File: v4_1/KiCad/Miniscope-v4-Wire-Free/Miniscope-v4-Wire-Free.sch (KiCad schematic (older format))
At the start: 92 parts, among them J1 0475710001, J10 Conn_01x01, J2 Conn_01x04, J3 Conn_01x04, J4 Conn_01x01, J5 Conn_01x01, J6 Conn_01x01, J7 Conn_01x01, J8 Conn_01x01, J9 Conn_01x01, Q1 NTK3134NT1G, U1 LTC3554, U2 HV892, U3 LTC3218, U4 MAX13030EETE+BGA, U5 TSOP57438TT1, U6 ATSAMD51J20A-UUT-EFP, U7 NCP163AMX330TBG, U8 NOIP1SN0480A, U9 LMV321IDCKR, Y1 Crystal_GND24, Y2 Crystal_GND24

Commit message: Start routing PCB v4 wire-free
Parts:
- removed C21, C8: 26pF, .Capacitor:C_0201_0603Metric_L, symbol .Device:C_Small
- removed C39: 1uF, .Capacitor:C_0201_0603Metric_L, symbol .Device:C_Small
- removed Y1, Y2: Crystal_GND24, Crystal:Crystal_SMD_2016-4Pin_2.0x1.6mm, symbol Device:Crystal_GND24
- added J14, J15, J16, J17, J18, J19, J20, J21, J22, J23, J24, J25, J26, J27: Conn_01x01, .Connector:Conn_1x1_700_Circular_Pad, symbol Connector_Generic:Conn_01x01
- added Y2: Crystal, Crystal:Crystal_SMD_MicroCrystal_CC8V-T1A-2Pin_2.0x1.2mm, symbol Device:Crystal
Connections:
- net labels added: I_LED, UART_RX, UART_TX
- net labels removed: SD_EN, USB_DM, USB_DP
- wire segments 356 -> 354
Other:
- note added: "Probably add volt div on output. Internal is a 33K res up to VSS"
- note added: "SERCOM5"
- moved on the sheet: C18, C20

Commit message: Do more routing
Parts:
- added D3: LED_Small_ALT, .LED:LED_SC80X160X65L40L, symbol .Device:LED_Small_ALT
- added J11, J12: Conn_01x01, .Connector:Conn_1x1_700_Circular_Pad, symbol Connector_Generic:Conn_01x01
- added R15: 37K, .Resistor:R_0201_0603Metric_ERJ_L, symbol .Device:R_Small_US
- added R16: 100K, .Resistor:R_0201_0603Metric_ERJ_L, symbol .Device:R_Small_US
- added R17: 25K, .Resistor:R_0201_0603Metric_ERJ_L, symbol .Device:R_Small_US
- added R18: R_Small_US, .Resistor:R_0201_0603Metric_ERJ_L, symbol .Device:R_Small_US
- added SW1: TL3780AF330QG, .Switch:SMD-Switch-3mmx2mm, symbol Switch:SW_Push
- D2: footprint (none) -> .LED:LED_SC80X160X65L40L
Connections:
- net USB_D+ is gone; now on net PUSH_BUT_MCU: U6.A1 (PA25)
- net USB_D- is gone; now on net STBY_POWER: U6.B1 (PA24)
- net XIN is gone; now on net IR_REC: U6.A2 (PB22)
- net +1V8: now also J6.1 (Pin_1), U1.9 (PWR_ON1), R16.1; no longer J7.1 (Pin_1)
- net +3V3: now also U1.8 (PWR_ON2), D3.2 (A)
- net BAT+: now also J10.1 (Pin_1); no longer J9.1 (Pin_1)
- net GND: now also J1.G4 (POL), J5.1 (Pin_1), J9.1 (Pin_1), U1.2 (FSEL), J11.1 (Pin_1), J12.1 (Pin_1), R15.2, R18.1, SW1.1; no longer J10.1 (Pin_1), J20.1 (Pin_1), J27.1 (Pin_1), J4.1 (Pin_1)
- net IR_REC: now also R15.1
- net MONITOR0: now also U6.G8 (PA07)
- net RESET_N: now also U6.H4 (PB13)
- net SWCLK: now also J7.1 (Pin_1); no longer J5.1 (Pin_1)
- net SWDIO: now also J4.1 (Pin_1); no longer J6.1 (Pin_1)
- net TRIGGER0: now also U6.H2 (PA15)
- net USB_VBUS: now also R17.2
- net SD_DET: now reaches J1.G5 (DET)
- net SD_DET: now also U6.F8 (PB09)
- net LED_STATUS: now reaches U6.D8 (PB05)
- net at U1.1 (HPWR): now also R17.1
- net STBY_POWER: now reaches U1.10 (STBY)
- net PUSH_BUT_MCU: now reaches U1.3 (PBSTAT)
- net PUSH_BUT_MCU: now also R16.2
- net nON: now reaches U1.5 (nON)
- net nON: now also J20.1 (Pin_1), J27.1 (Pin_1), SW1.2
- net XOUT: no longer names the net of U6.A3 (PB23)
- new net: D3.1 (K), R18.2
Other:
- note added: "Can use side mount LED \nLTST-S270KRKT"
- note added: "Int. pull down res"
- moved on the sheet: J10, J9

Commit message: Finish most of the routing.
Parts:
- added Q2: MMBT3904LP-7B, .Transistor:TRXDFN3_101X61X53L25X15N, symbol .Transistor:MMBT3904LP-7B
- added R19: 1K, .Resistor:R_0201_0603Metric_ERJ_L, symbol .Device:R_Small_US
- added R20: 100K, .Resistor:R_0201_0603Metric_ERJ_L, symbol .Device:R_Small_US
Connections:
- net +1V8: now also J19.1 (Pin_1), J26.1 (Pin_1), R20.2; no longer J15.1 (Pin_1), J22.1 (Pin_1)
- net +3V3: no longer U1.8 (PWR_ON2)
- net GND: now also U1.10 (STBY), Q2.2 (E)
- net I2C_BB_SCL: now also J15.1 (Pin_1), J22.1 (Pin_1); no longer J17.1 (Pin_1), J24.1 (Pin_1)
- net I2C_BB_SDA: now also J16.1 (Pin_1), J23.1 (Pin_1); no longer J18.1 (Pin_1), J25.1 (Pin_1)
- net IR_REC: now also J17.1 (Pin_1), J24.1 (Pin_1); no longer J19.1 (Pin_1), J26.1 (Pin_1)
- net I_LED: now also J18.1 (Pin_1), J25.1 (Pin_1); no longer J16.1 (Pin_1), J23.1 (Pin_1)
- net LED_STATUS: now also U6.F8 (PB09), R19.2; no longer U6.D8 (PB05)
- net SD_DET: now also U6.D8 (PB05); no longer U6.F8 (PB09)
- net UART_RX: now also J2.2 (Pin_2); no longer J2.3 (Pin_3)
- net UART_TX: now also J2.3 (Pin_3); no longer J2.2 (Pin_2)
- net VDC: now also R2.2; no longer D2.2 (A)
- net nCHRG: now reaches U6.A3 (PB23)
- net nCHRG: now also U1.14 (nCHRG), R20.1
- net at R2.1: now also D2.2 (A); no longer D2.1 (K)
- net STBY_POWER renamed 3V3_EN
- net 3V3_EN: now also U1.8 (PWR_ON2); no longer U1.10 (STBY)
- new net: D2.1 (K), Q2.3 (C)
- new net: Q2.1 (B), R19.1
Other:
- note added: "Use EXTINT"
- moved on the sheet: D2, R2
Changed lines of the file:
@@
 	3150 2950 3500 2950
 Connection ~ 3500 2950
-Wire Wire Line
-	3500 2950 3800 2950
 $Comp
 L .Device:C_Small C1
@@
 L .Device:R_Small_US R2
 U 1 1 60DF8071
-P 3050 3300
-F 0 "R2" V 2950 3300 50  0000 C CNN
-F 1 "R_Small_US" V 3150 3400 50  0000 C CNN
-F 2 ".Resistor:R_0201_0603Metric_ERJ_L" H 3050 3300 50  0001 C CNN
-F 3 "~" H 3050 3300 50  0001 C CNN
-	1    3050 3300
-	0    1    1    0
-$EndComp
-Wire Wire Line
-	2800 3300 2950 3300
+P 3800 9550
+F 0 "R2" V 3700 9550 50  0000 C CNN
+F 1 "R_Small_US" V 3950 9550 50  0000 C CNN
+F 2 ".Resistor:R_0201_0603Metric_ERJ_L" H 3800 9550 50  0001 C CNN
+F 3 "~" H 3800 9550 50  0001 C CNN
+	1    3800 9550
+	-1   0    0    1
+$EndComp
 $Comp
 L .Device:LED_Small_ALT D2
 U 1 1 60E08DD6
-P 3400 3300
-F 0 "D2" H 3500 3350 50  0000 C CNN
-F 1 "LED_Small_ALT" H 3750 3200 50  0000 C CNN
-F 2 ".LED:LED_SC80X160X65L40L" V 3400 3300 50  0001 C CNN
-F 3 "~" V 3400 3300 50  0001 C CNN
-	1    3400 3300
-	1    0    0    -1
-$EndComp
-Wire Wire Line
-	3300 3300 3150 3300
-Wire Wire Line
-	3500 3300 3800 3300
-Wire Wire Line
-	3800 3300 3800 2950
-Connection ~ 3800 2950
-Wire Wire Line
-	3800 2950 3900 2950
+P 3800 10000
+F 0 "D2" H 3800 10125 50  0000 C CNN
+F 1 "LED_Small_ALT" H 3800 9850 50  0000 C CNN
+F 2 ".LED:LED_SC80X160X65L40L" V 3800 10000 50  0001 C CNN
+F 3 "~" V 3800 10000 50  0001 C CNN
+	1    3800 10000
+	0    -1   -1   0
+$EndComp
 Wire Wire Line
 	4400 3700 4700 3700
@@
 $EndComp
 Wire Wire Line
-	12625 12625 12300 12625
-Wire Wire Line
 	12100 12725 12625 12725
 Wire Wire Line
 	12625 12825 12100 12825
-Wire Wire Line
-	12100 12925 12625 12925
 $Comp
 L power:+1V8 #PWR02
 U 1 1 610C48FA
-P 12300 12625
-F 0 "#PWR02" H 12300 12475 50  0001 C CNN
-F 1 "+1V8" H 12315 12798 50  0000 C CNN
-F 2 "" H 12300 12625 50  0001 C CNN
-F 3 "" H 12300 12625 50  0001 C CNN
-	1    12300 12625
-	1    0    0    -1
-$EndComp
-Connection ~ 12300 12625
-Wire Wire Line
-	12300 12625 12100 12625
+P 12225 13025
+F 0 "#PWR02" H 12225 12875 50  0001 C CNN
+F 1 "+1V8" H 12240 13198 50  0000 C CNN
+F 2 "" H 12225 13025 50  0001 C CNN
+F 3 "" H 12225 13025 50  0001 C CNN
+	1    12225 13025
+	1    0    0    -1
+$EndComp
 Text Label 20525 2500 0    50   ~ 0
 I_LED
-Text Label 12225 12725 0    50   ~ 0
+Text Label 12225 12925 0    50   ~ 0
 I_LED
-Text Label 12150 12825 0    50   ~ 0
+Text Label 12150 12625 0    50   ~ 0
 I2C_BB_SCL
-Text Label 12150 12925 0    50   ~ 0
+Text Label 12150 12725 0    50   ~ 0
 I2C_BB_SDA
 $Comp
@@
 Text Label 6525 7375 0    50   ~ 0
 IR_REC
-Text Label 12475 13025 2    50   ~ 0
+Text Label 12400 12825 2    50   ~ 0
 IR_REC
 Wire Wire Line
@@
 	12150 12525 12625 12525
 Wire Wire Line
-	12100 13025 12625 13025
+	12100 13025 12225 13025
 Wire Wire Line
 	6525 8175 7125 8175
@@
 Text Notes 6150 8250 0    50   ~ 0
 SERCOM5
+Text Label 1950 1250 2    50   ~ 0
+UART_RX
 Text Label 1950 1150 2    50   ~ 0
-UART_RX
-Text Label 1950 1250 2    50   ~ 0
 UART_TX
 Wire Wire Line
@@
 USB_VBUS
 Wire Wire Line
-	1700 4250 900  4250
+	1700 4250 1100 4250
 $Comp
 L power:GND #PWR0143
@@
 Wire Wire Line
 	1700 4350 1100 4350
-Text Label 1100 4350 0    50   ~ 0
-STBY_POWER
 Text Notes 975  3725 0    50   ~ 0
 Int. pull down res
@@
 	1    0    0    -1
 $EndComp
-$Comp
-L power:+3.3V #PWR01
-U 1 1 61CFAB69
-P 3425 5150
-F 0 "#PWR01" H 3425 5000 50  0001 C CNN
-F 1 "+3.3V" H 3400 5300 50  0000 C CNN
-F 2 "" H 3425 5150 50  0001 C CNN
-F 3 "" H 3425 5150 50  0001 C CNN
-	1    3425 5150
-	1    0    0    -1
-$EndComp
-Text Notes 3900 3350 0    50   ~ 0
+Text Notes 3150 3475 0    50   ~ 0
 Can use side mount LED 	\nLTST-S270KRKT
 $Comp
@@
 	1    0    0    -1
 $EndComp
-$Comp
-L power:+3.3V #PWR0148
-U 1 1 61DDE71F
-P 1100 4050
-F 0 "#PWR0148" H 1100 3900 50  0001 C CNN
-F 1 "+3.3V" H 1075 4200 50  0000 C CNN
-F 2 "" H 1100 4050 50  0001 C CNN
-F 3 "" H 1100 4050 50  0001 C CNN
-	1    1100 4050
-	1    0    0    -1
-$EndComp
 Text Label 9525 7375 2    50   ~ 0
-STBY_POWER
+3V3_EN
 Wire Wire Line
 	8925 9875 9525 9875
@@
 Wire Wire Line
 	6525 8475 7125 8475
+Text Label 6525 8875 0    50   ~ 0
+LED_STATUS
 Text Label 6525 8475 0    50   ~ 0
-LED_STATUS
-Text Label 6525 8875 0    50   ~ 0
 SD_DET
 Text Label 9525 9675 2    50   ~ 0
 MONITOR0
+Wire Wire Line
+	1100 4350 1100 4250
+Connection ~ 1100 4250
+Wire Wire Line
+	1100 4250 900  4250
+Text Label 1100 4050 0    50   ~ 0
+3V3_EN
+Connection ~ 12225 13025
+Wire Wire Line
+	12225 13025 12625 13025
+$Comp
+L .Transistor:MMBT3904LP-7B Q2
+U 1 1 624E582C
+P 3700 10500
+F 0 "Q2" H 3891 10546 50  0000 L CNN
+F 1 "MMBT3904LP-7B" H 3891 10455 50  0000 L CNN
+F 2 ".Transistor:TRXDFN3_101X61X53L25X15N" H 3900 10425 50  0001 L CIN
+F 3 "https://www.diodes.com/assets/Datasheets/ds31835.pdf" H 3700 10500 50  0001 L CNN
+	1    3700 10500
+	1    0    0    -1
+$EndComp
+Wire Wire Line
+	12100 12625 12625 12625
+Wire Wire Line
+	12100 12925 12625 12925
+Wire Wire Line
+	3800 10700 3800 10825
+Wire Wire Line
+	3800 10300 3800 10100
+Wire Wire Line
+	3800 9450 3800 9350
+$Comp
+L power:GND #PWR07
+U 1 1 62611F8B
+P 3800 10825
+F 0 "#PWR07" H 3800 10575 50  0001 C CNN
+F 1 "GND" H 3850 10625 50  0000 C CNN
+F 2 "" H 3800 10825 50  0001 C CNN
+F 3 "" H 3800 10825 50  0001 C CNN
+	1    3800 10825
+	1    0    0    -1
+$EndComp
+$Comp
+L .Device:R_Small_US R19
+U 1 1 62614175
+P 3225 10500
+F 0 "R19" V 3325 10400 50  0000 L CNN
+F 1 "1K" V 3300 10550 50  0000 L CNN
+F 2 ".Resistor:R_0201_0603Metric_ERJ_L" H 3225 10500 50  0001 C CNN
+F 3 "~" H 3225 10500 50  0001 C CNN
+	1    3225 10500
+	0    1    1    0
+$EndComp
+Wire Wire Line
+	3500 10500 3325 10500
+Wire Wire Line
+	3125 10500 2625 10500
+Text Label 2625 10500 0    50   ~ 0
+LED_STATUS
+$Comp
+L power:VDC #PWR06
+U 1 1 6270EC46
+P 3800 9350
+F 0 "#PWR06" H 3800 9250 50  0001 C CNN
+F 1 "VDC" H 3900 9550 50  0000 C CNN
+F 2 "" H 3800 9350 50  0001 C CNN
+F 3 "" H 3800 9350 50  0001 C CNN
+	1    3800 9350
+	1    0    0    -1
+$EndComp
+Wire Wire Line
+	3800 9650 3800 9900
+Wire Wire Line
+	3500 2950 3900 2950
+Wire Wire Line
+	2800 3300 4300 3300
+$Comp
+L .Device:R_Small_US R20
+U 1 1 62800A4A
+P 4300 3200
+F 0 "R20" V 4200 3200 50  0000 C CNN
+F 1 "100K" V 4400 3200 50  0000 C CNN
+F 2 ".Resistor:R_0201_0603Metric_ERJ_L" H 4300 3200 50  0001 C CNN
+F 3 "~" H 4300 3200 50  0001 C CNN
+	1    4300 3200
+	-1   0    0    1
+$EndComp
+Wire Wire Line
+	4300 3100 4300 3025
+$Comp
+L power:+1V8 #PWR011
+U 1 1 6283B8D8
+P 4300 3025
+F 0 "#PWR011" H 4300 2875 50  0001 C CNN
+F 1 "+1V8" H 4400 3225 50  0000 C CNN
+F 2 "" H 4300 3025 50  0001 C CNN
+F 3 "" H 4300 3025 50  0001 C CNN
+	1    4300 3025
+	1    0    0    -1
+$EndComp
+$Comp
+L power:+3.3V #PWR0148
+U 1 1 62844F10
+P 3425 5150
+F 0 "#PWR0148" H 3425 5000 50  0001 C CNN
+F 1 "+3.3V" H 3525 5350 50  0000 C CNN
+F 2 "" H 3425 5150 50  0001 C CNN
+F 3 "" H 3425 5150 50  0001 C CNN
+	1    3425 5150
+	1    0    0    -1
+$EndComp
+Text Label 3825 3300 0    50   ~ 0
+nCHRG
+Text Label 6525 7475 0    50   ~ 0
+nCHRG
+Text Notes 6050 7375 0    50   ~ 0
+Use EXTINT
 $EndSCHEMATC

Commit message: routing almost done.
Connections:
- net EWL_1: now also J3.4 (Pin_4)
- net EWL_2: now also J3.1 (Pin_1)
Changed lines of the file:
@@
 EWL_2
 Wire Wire Line
-	20800 7950 21400 7950
-Wire Wire Line
-	20800 8050 21400 8050
+	20800 7950 21340 7950
+Wire Wire Line
+	20800 8050 21340 8050
 Text Label 20800 8050 0    50   ~ 0
 EWL_1
@@
 Text Notes 6050 7375 0    50   ~ 0
 Use EXTINT
+Wire Wire Line
+	21400 7850 21340 7850
+Wire Wire Line
+	21340 7850 21340 7950
+Connection ~ 21340 7950
+Wire Wire Line
+	21340 7950 21400 7950
+Wire Wire Line
+	21340 8050 21340 8150
+Wire Wire Line
+	21340 8150 21400 8150
+Connection ~ 21340 8050
+Wire Wire Line
+	21340 8050 21400 8050
 $EndSCHEMATC

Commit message: Minor corrections
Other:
- note added: "Capabilities:\n* Battery monitoring\n* IR Receiver\n* Power supply shutdown and low power mode\n* Push button on/reset and user input\n* Power LED, excitation LED, status LED\n* Onboard charger\n* UART connection for wired operation\n* EWL flex cable connector\n* Dynamic clock adjustment for MCU and image sensor\n* Low power EWL driver\n* Pogo pin SWD interface"
- note added: "Internal is a 33K res up to VS"
- note added: "UART Connector"
- note removed: "1.8v, 3.3v, VDC, gnd, sda, slc, ENT, PWM, 6sd"
- note removed: "NEED BATTERY CONNECTION"
- note removed: "Probably add volt div on output. Internal is a 33K res up to VSS"
- note removed: "USB Connector"
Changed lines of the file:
@@
 	900  1600 900  700
 Text Notes 1300 650  0    50   ~ 0
-USB Connector
+UART Connector
 Wire Wire Line
 	19950 11550 20700 11550
@@
 Text Label 3150 7450 2    50   ~ 0
 IR_REC
-Text Notes 3000 850  0    50   ~ 0
-1.8v, 3.3v, VDC, gnd, sda, slc, ENT, PWM, 6sd
-Text Notes 3050 1350 0    50   ~ 0
-NEED BATTERY CONNECTION
 Wire Notes Line
 	1700 6800 3200 6800
@@
 Wire Wire Line
 	2400 7850 2550 7850
-Text Notes 1100 8225 0    50   ~ 0
-Probably add volt div on output. Internal is a 33K res up to VSS
+Text Notes 1955 8185 0    50   ~ 0
+Internal is a 33K res up to VS
 $Comp
 L power:+3.3V #PWR0130
@@
 Wire Wire Line
 	21340 8050 21400 8050
+Text Notes 725  15890 0    157  ~ 0
+Capabilities:\n* Battery monitoring\n* IR Receiver\n* Power supply shutdown and low power mode\n* Push button on/reset and user input\n* Power LED, excitation LED, status LED\n* Onboard charger\n* UART connection for wired operation\n* EWL flex cable connector\n* Dynamic clock adjustment for MCU and image sensor\n* Low power EWL driver\n* Pogo pin SWD interface
 $EndSCHEMATC

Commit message: Create MCU firmware project
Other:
- note added: "ADC0 | AIN/0"
- note added: "GCLK_IO[1]"
- note added: "PCC peripheral clock must be > 2x PCC_CLK"
- note added: "SPI -> SERCOM0"
- note added: "TCO, WO/0"
- note added: "Use EXTINT[6]"
- note added: "Use EXTINT[7]"
- note removed: "Use EXTINT"
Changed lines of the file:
@@
 Text Label 7125 2550 0    50   ~ 0
 VDDCORE
-Text Notes 9575 8025 0    50   ~ 0
+Text Notes 10200 7980 0    50   ~ 0
 Internal vref bandgap = 1.1V
 Wire Wire Line
@@
 Text Label 6525 7475 0    50   ~ 0
 nCHRG
-Text Notes 6050 7375 0    50   ~ 0
-Use EXTINT
+Text Notes 5890 7370 0    50   ~ 0
+Use EXTINT[6]
 Wire Wire Line
 	21400 7850 21340 7850
@@
 Text Notes 725  15890 0    157  ~ 0
 Capabilities:\n* Battery monitoring\n* IR Receiver\n* Power supply shutdown and low power mode\n* Push button on/reset and user input\n* Power LED, excitation LED, status LED\n* Onboard charger\n* UART connection for wired operation\n* EWL flex cable connector\n* Dynamic clock adjustment for MCU and image sensor\n* Low power EWL driver\n* Pogo pin SWD interface
+Text Notes 5990 9465 0    50   ~ 0
+GCLK_IO[1]
+Text Notes 9635 9060 0    50   ~ 0
+SPI -> SERCOM0
+Text Notes 9580 7980 0    50   ~ 0
+ADC0 | AIN/0
+Text Notes 6060 7570 0    50   ~ 0
+TCO, WO/0
+Text Notes 9580 9770 0    50   ~ 0
+PCC peripheral clock must be > 2x PCC_CLK
+Text Notes 5895 7480 0    50   ~ 0
+Use EXTINT[7]
 $EndSCHEMATC

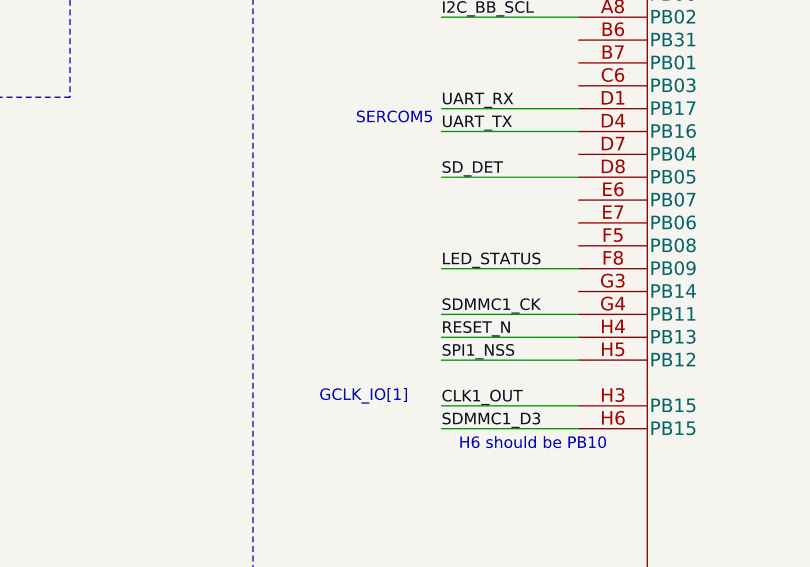
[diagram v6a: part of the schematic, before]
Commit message: Add frame valid additional pin and external int to MCU.
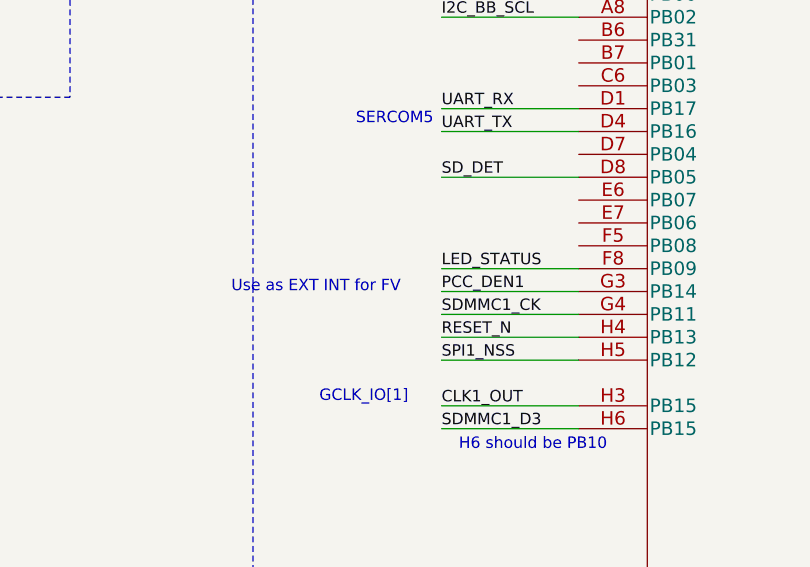
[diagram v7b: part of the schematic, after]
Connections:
- net PCC_DEN1: now also U6.G3 (PB14)
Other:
- note added: "Use as EXT INT for FV"
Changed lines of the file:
@@
 Text Notes 5895 7480 0    50   ~ 0
 Use EXTINT[7]
+Wire Wire Line
+	6525 8975 7125 8975
+Text Label 6525 8975 0    50   ~ 0
+PCC_DEN1
+Text Notes 5605 8985 0    50   ~ 0
+Use as EXT INT for FV
 $EndSCHEMATC

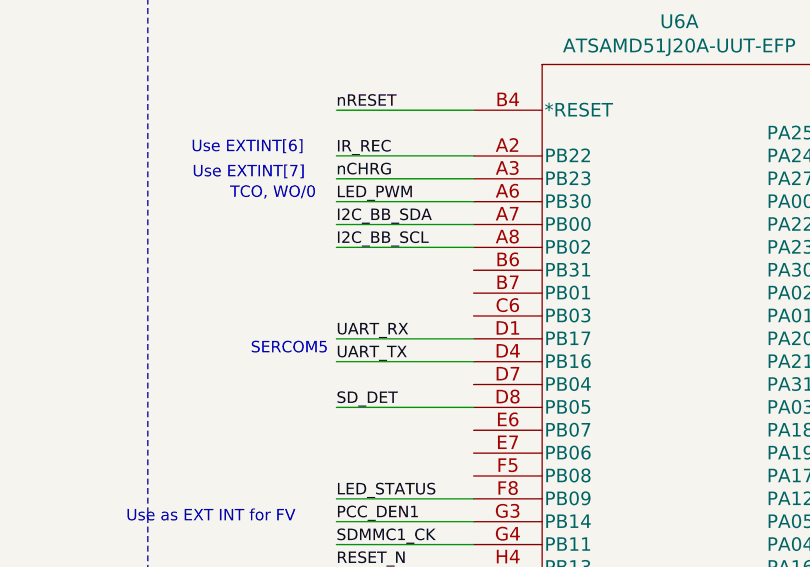
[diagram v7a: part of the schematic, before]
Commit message: Add ENT connection on PCB. Start fleshing out MCU code.
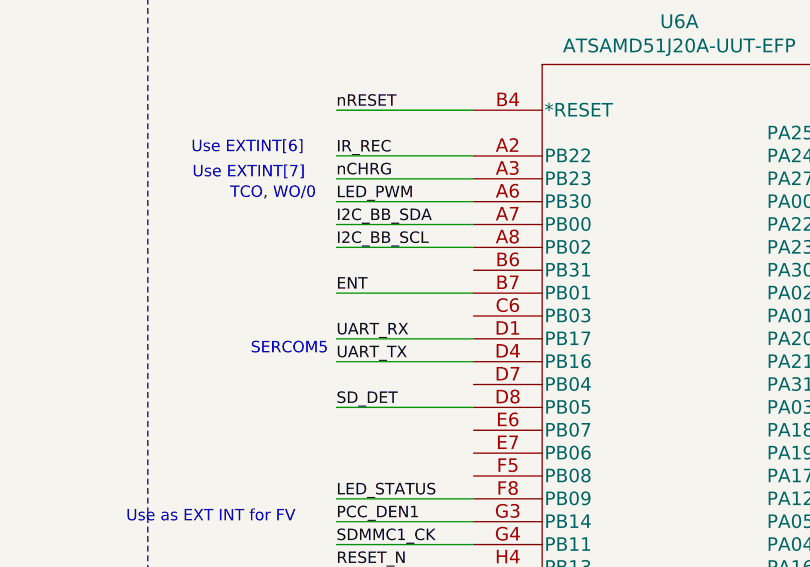
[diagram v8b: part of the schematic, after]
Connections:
- net ENT: now also U6.B7 (PB01)
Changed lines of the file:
@@
 Text Notes 5605 8985 0    50   ~ 0
 Use as EXT INT for FV
+Text Label 6525 7975 0    50   ~ 0
+ENT
+Wire Wire Line
+	6525 7975 7125 7975
 $EndSCHEMATC
